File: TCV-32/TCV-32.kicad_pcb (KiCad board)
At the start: 2 copper layers, 218.8 x 130.2 mm, 58 parts, among them J1 Screw_Terminal_01x02, J2 Screw_Terminal_01x02, J3 Screw_Terminal_01x02, J4 Servomotor, J5 LM393, J6 Servomotor, U2 L7805, U3 L293D, U4 DEVKIT_V1_ESP32-WROOM-32

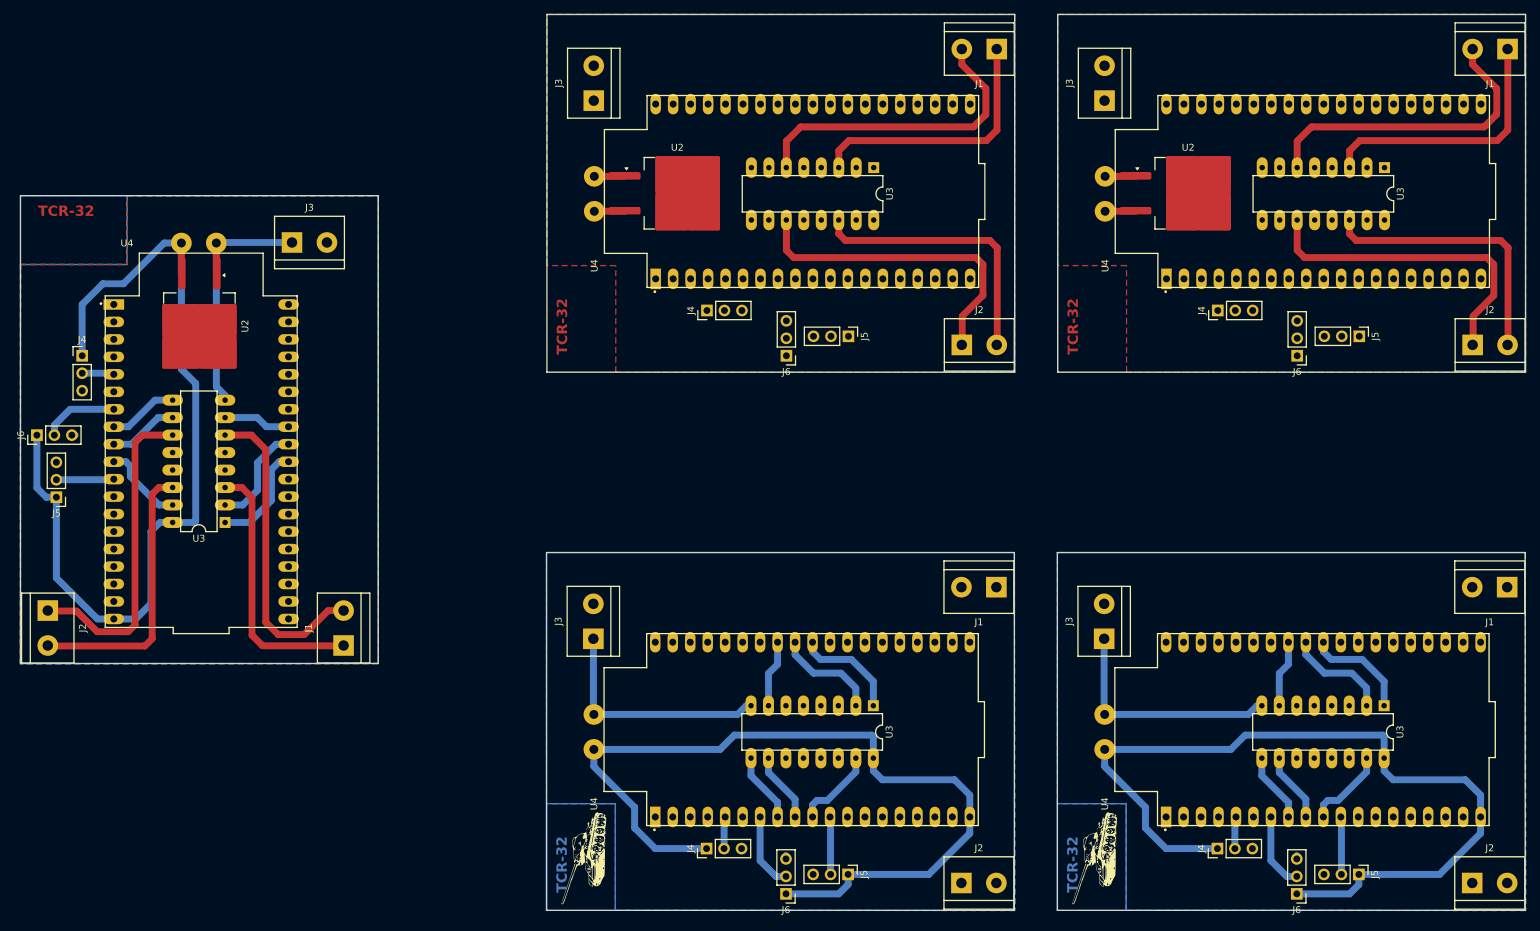
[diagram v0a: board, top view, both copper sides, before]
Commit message: Cambio de componentes
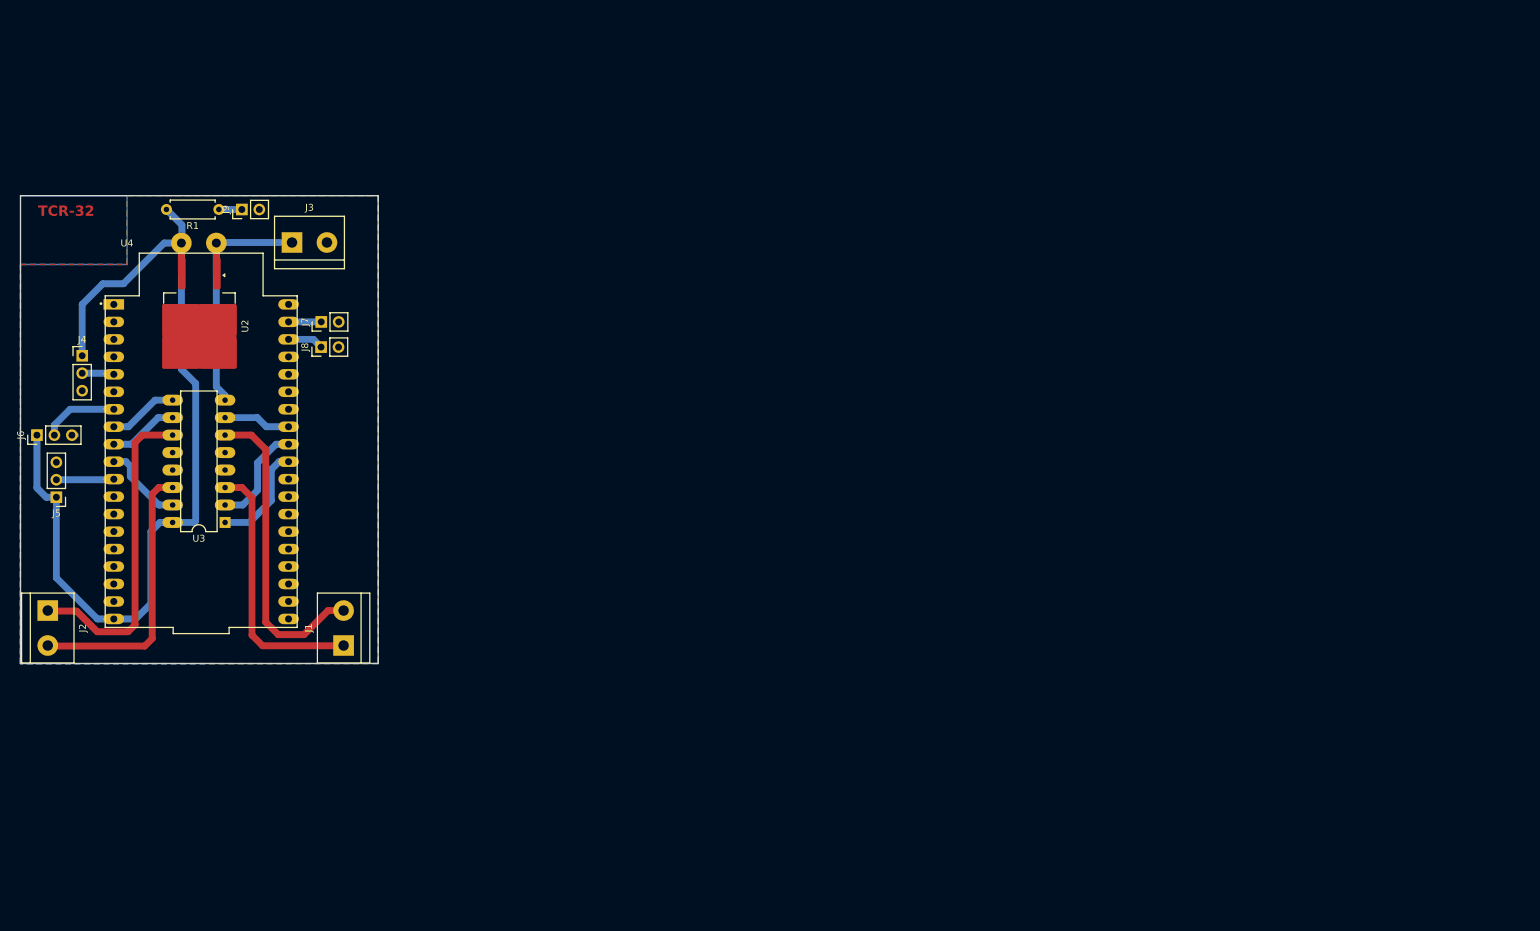
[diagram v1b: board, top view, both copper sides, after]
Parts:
- removed the ? at (167.2, 46.9)
- removed the ? at (92.9, 125.2)
- removed the ? at (92.9, 52.0)
- removed the ? at (92.9, 130.2)
- removed the ? at (92.9, 46.9)
- removed the ? at (167.1, 130.2)
- removed the ? at (167.2, 52.0)
- removed the ? at (167.1, 125.2)
- removed the G*** at (90.9, 146.2)
- removed the G*** at (165.2, 146.2)
- removed the G*** at (165.2, 68.0)
- removed the G*** at (91.0, 68.0)
- removed the J1 at (151.4, 106.7)
- removed the J1 at (151.4, 28.4)
- removed the J1 at (225.6, 106.7)
- removed the J1 at (225.7, 28.4)
- removed the J2 at (220.6, 71.4)
- removed the J2 at (220.6, 149.7)
- removed the J2 at (146.3, 149.7)
- removed the J2 at (146.4, 71.4)
- removed the J3 at (167.1, 114.2)
- removed the J3 at (167.1, 35.9)
- removed the J3 at (92.9, 35.9)
- removed the J3 at (92.8, 114.2)
- removed the J4 at (109.3, 144.7)
- removed the J4 at (183.5, 144.7)
- removed the J4 at (109.3, 66.4)
- removed the J4 at (183.6, 66.4)
- removed the J5 at (204.1, 70.2)
- removed the J5 at (204.1, 148.4)
- removed the J5 at (129.8, 148.4)
- removed the J5 at (129.9, 70.2)
- removed the J6 at (195.1, 151.2)
- removed the J6 at (120.9, 73.0)
- removed the J6 at (120.8, 151.2)
- removed the J6 at (195.1, 73.0)
- removed the U2 at (105.0, 49.4)
- removed the U2 at (179.3, 49.4)
- removed the U3 at (207.8, 45.7)
- removed the U3 at (133.6, 45.7)
- removed the U3 at (207.8, 123.9)
- removed the U3 at (133.5, 123.9)
- removed the U4 at (124.7, 49.1)
- removed the U4 at (124.7, 127.3)
- removed the U4 at (198.9, 127.3)
- removed the U4 at (199.0, 49.1)
- added J7: Conn_01x02_Pin, Connector_PinHeader_2.54mm:PinHeader_1x02_P2.54mm_Vertical, F.Cu at (53.2, 68.1)
- added J8: Conn_01x02_Pin, Connector_PinHeader_2.54mm:PinHeader_1x02_P2.54mm_Vertical, F.Cu at (53.2, 71.8)
- added J9: Conn_01x02_Pin, Connector_PinHeader_2.54mm:PinHeader_1x02_P2.54mm_Vertical, F.Cu at (41.7, 51.8)
- added R1: R, Resistor_THT:R_Axial_DIN0207_L6.3mm_D2.5mm_P7.62mm_Horizontal, F.Cu at (38.4, 51.8)
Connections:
- U4 pad 36: unconnected-(U4-IO22-Pad36) -> L2
- U4 pad 37: unconnected-(U4-IO23-Pad37) -> L1
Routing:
- net +5V: track 386.5 -> 134.7 mm
- net Net-(J2-Pin_1): track 140.4 -> 46.8 mm
- net Net-(J1-Pin_2): track 136.2 -> 45.4 mm
- net Net-(J2-Pin_2): track 120.1 -> 40.0 mm
- net +: track 116.5 -> 38.8 mm
- net Net-(J1-Pin_1): track 115.5 -> 38.5 mm
- net A3: track 46.6 -> 15.5 mm
- net A1: track 45.7 -> 15.2 mm
- net B1: track 36.1 -> 12.0 mm
- net Sr2: track 33.2 -> 11.1 mm
- net B3: track 30.5 -> 10.2 mm
- net B2: track 30.5 -> 10.2 mm
- net A2: track 29.3 -> 9.78 mm
- net OUT: track 25.2 -> 8.39 mm
- net Sr1: track 14.0 -> 4.67 mm
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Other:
- board size 218.8 x 130.2 mm -> 52 x 68 mm
